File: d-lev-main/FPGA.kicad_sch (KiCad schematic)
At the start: 6 parts, among them J2 Tag-Connect TC2030-NL, U3 AC608, U4 25LCxxx

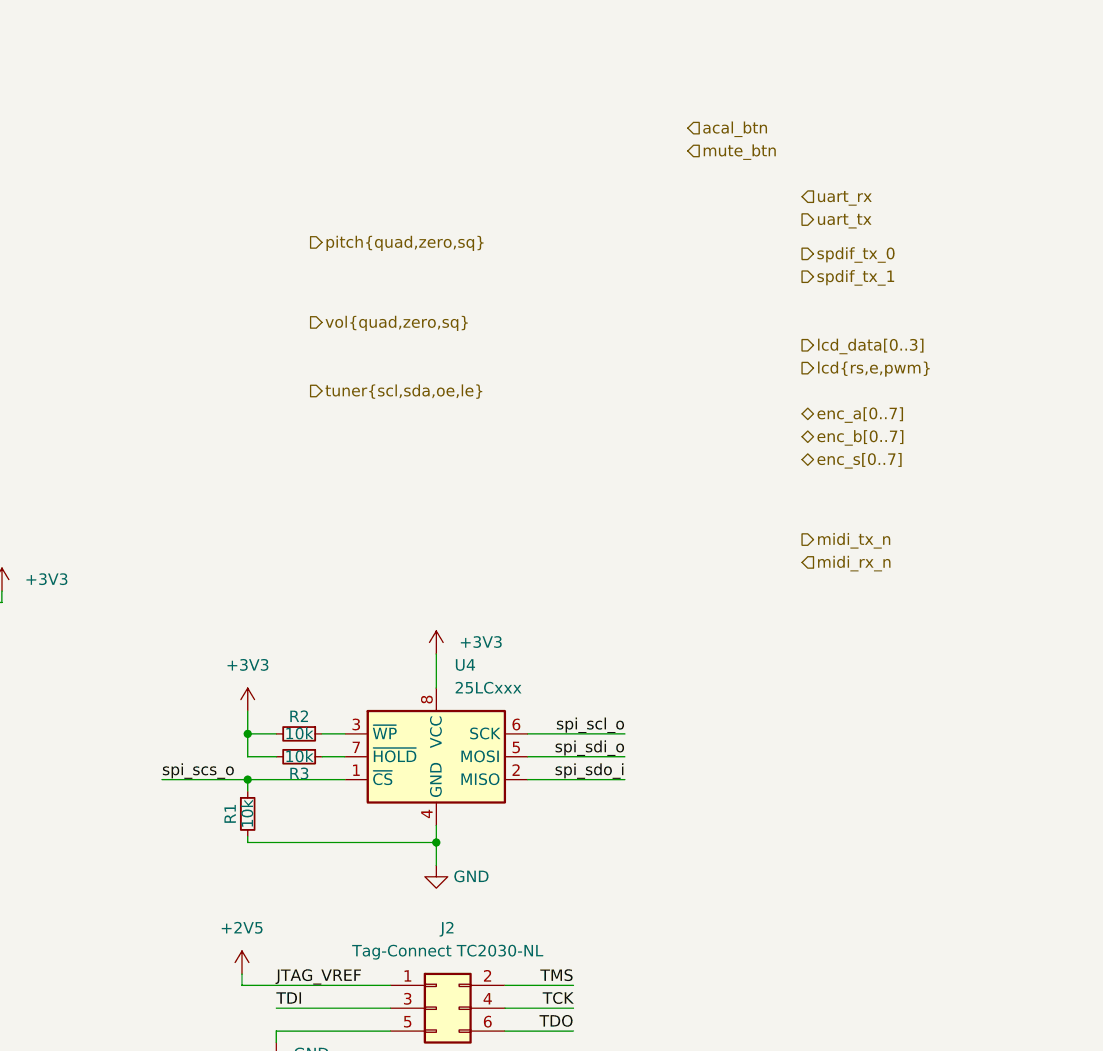
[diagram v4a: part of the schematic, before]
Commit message: Level shifters and rearrange encoders
* WIP: use net buses more effectively to organize encoder signals
* Add application note for level shifters
* Add level shifters for UART, change MIDI level shifter BJT to FET
* Add MIDI_HI pull-up on d-lev-io board
* Add/change some footprints
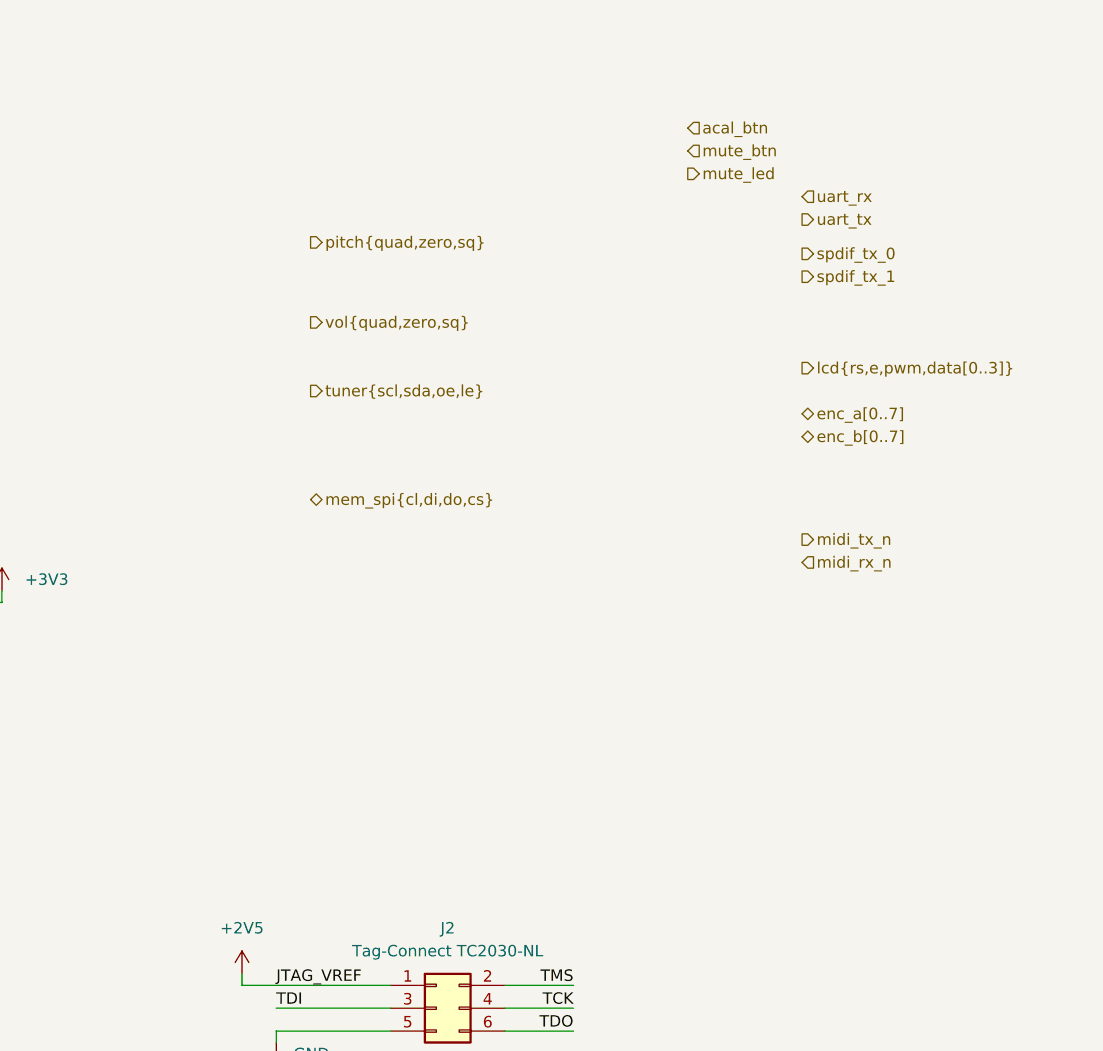
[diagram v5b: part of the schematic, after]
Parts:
- removed R1, R2, R3: 10k, symbol Device:R_Small
- removed U4: 25LCxxx, Package_SO:SOIC-8W_5.3x5.3mm_P1.27mm, symbol Memory_EEPROM:25LCxxx

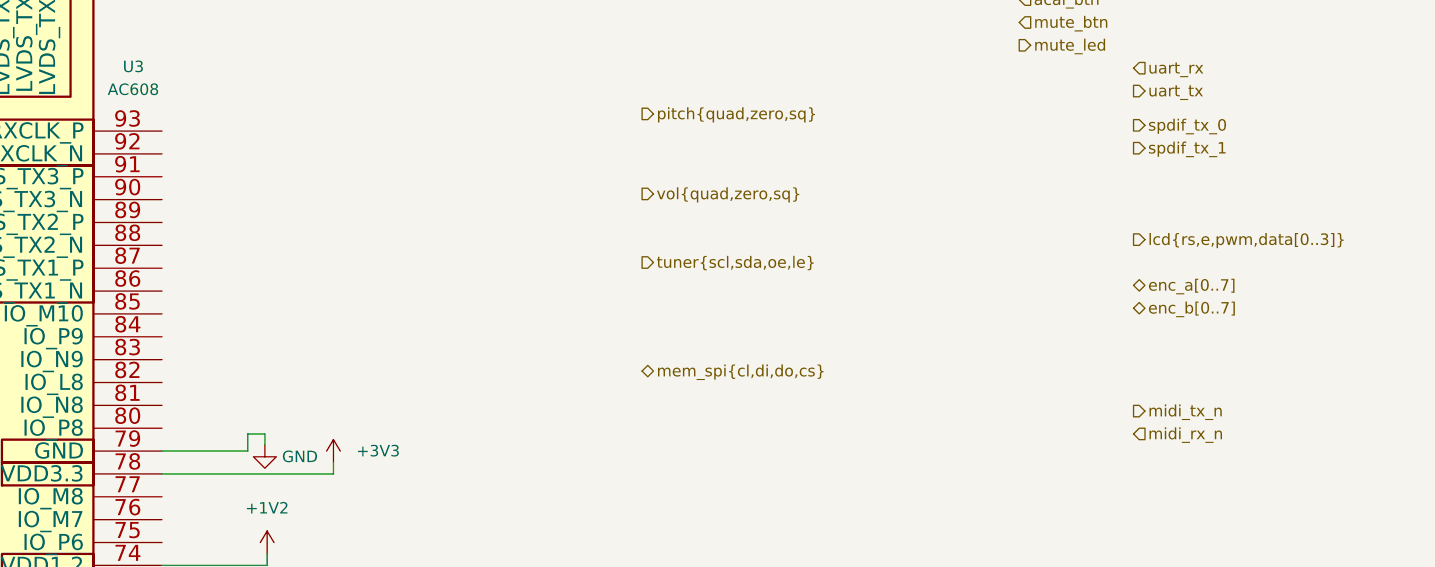
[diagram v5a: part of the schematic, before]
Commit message: more encoder bus mangling
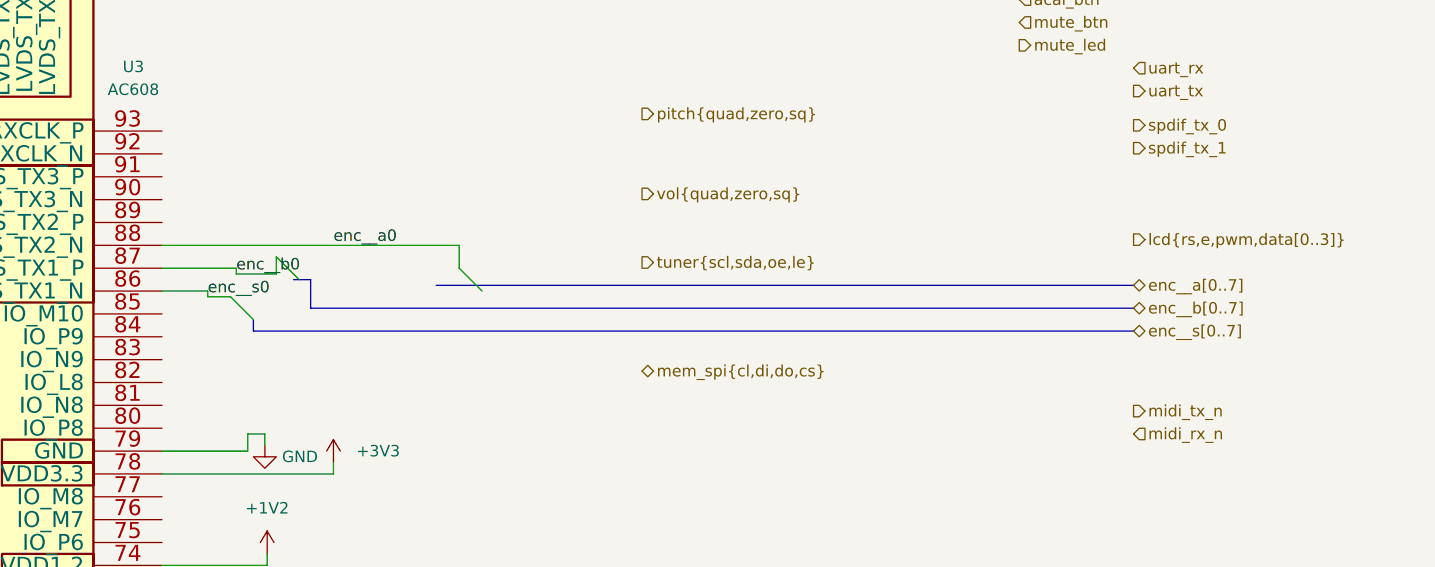
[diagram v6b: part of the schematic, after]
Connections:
- net enc__s0: now reaches U3.86 (LVDS_TX1_N)
- net enc__b0: now reaches U3.87 (LVDS_TX1_P)
- net enc__a0: now reaches U3.88 (LVDS_TX2_N)
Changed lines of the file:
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@@
 (kicad_sch (version 20230121) (generator eeschema)
   (paper "A4")
+  (bus_alias "lcdpins" (members "lcd{rs,e,pwm,data[0..3]}"))
   (bus_alias "tuner" (members "scl" "sda" "oe" "le"))
-  (bus_alias "lcdpins" (members "lcd{rs,e,pwm,data[0..3]}"))
+  (bus_entry (at 158.75 81.915) (size -2.54 -2.54)
+    (stroke (width 0) (type default))
+  )
+  (bus_entry (at 179.07 83.185) (size -2.54 -2.54)
+    (stroke (width 0) (type default))
+  )
+  (bus_entry (at 153.67 86.36) (size -2.54 -2.54)
+    (stroke (width 0) (type default))
+  )
+  (wire (pts (xy 156.21 79.375) (xy 156.21 81.28))
+    (stroke (width 0) (type default))
+  )
   (wire (pts (xy 218.44 151.13) (xy 226.06 151.13))
     (stroke (width 0) (type default))
@@
     (stroke (width 0) (type default))
   )
+  (wire (pts (xy 156.21 81.28) (xy 151.765 81.28))
+    (stroke (width 0) (type default))
+  )
   (wire (pts (xy 155.194 113.665) (xy 155.194 112.395))
     (stroke (width 0) (type default))
@@
     (stroke (width 0) (type default))
   )
+  (wire (pts (xy 151.765 80.645) (xy 151.765 81.28))
+    (stroke (width 0) (type default))
+  )
+  (wire (pts (xy 148.59 83.185) (xy 148.59 83.82))
+    (stroke (width 0) (type default))
+  )
+  (bus (pts (xy 251.46 87.63) (xy 153.67 87.63))
+    (stroke (width 0) (type default))
+  )
   (wire (pts (xy 100.33 36.195) (xy 100.33 37.465))
     (stroke (width 0) (type default))
   )
+  (bus (pts (xy 153.67 86.36) (xy 153.67 87.63))
+    (stroke (width 0) (type default))
+  )
   (wire (pts (xy 34.29 102.235) (xy 34.29 100.965))
     (stroke (width 0) (type default))
@@
     (stroke (width 0) (type default))
   )
+  (wire (pts (xy 176.53 80.645) (xy 176.53 78.105))
+    (stroke (width 0) (type default))
+  )
   (wire (pts (xy 92.71 175.895) (xy 92.71 174.625))
     (stroke (width 0) (type default))
@@
     (stroke (width 0) (type default))
   )
+  (wire (pts (xy 143.51 78.105) (xy 176.53 78.105))
+    (stroke (width 0) (type default))
+  )
   (wire (pts (xy 97.79 164.465) (xy 97.79 167.005))
     (stroke (width 0) (type default))
@@
     (stroke (width 0) (type default))
   )
+  (bus (pts (xy 158.75 81.915) (xy 160.02 81.915))
+    (stroke (width 0) (type default))
+  )
+  (bus (pts (xy 158.115 81.915) (xy 158.75 81.915))
+    (stroke (width 0) (type default))
+  )
+  (bus (pts (xy 251.46 85.09) (xy 160.02 85.09))
+    (stroke (width 0) (type default))
+  )
+  (wire (pts (xy 143.51 83.185) (xy 148.59 83.185))
+    (stroke (width 0) (type default))
+  )
   (wire (pts (xy 153.035 116.205) (xy 143.51 116.205))
     (stroke (width 0) (type default))
@@
     (stroke (width 0) (type default))
   )
+  (wire (pts (xy 143.51 80.645) (xy 151.765 80.645))
+    (stroke (width 0) (type default))
+  )
+  (wire (pts (xy 148.59 83.82) (xy 151.13 83.82))
+    (stroke (width 0) (type default))
+  )
   (wire (pts (xy 125.73 164.465) (xy 125.73 174.625))
     (stroke (width 0) (type default))
@@
     (stroke (width 0) (type default))
   )
+  (bus (pts (xy 160.02 85.09) (xy 160.02 81.915))
+    (stroke (width 0) (type default))
+  )
+  (bus (pts (xy 173.99 82.55) (xy 251.46 82.55))
+    (stroke (width 0) (type default))
+  )
   (label "TCK" (at 226.06 148.59 180) (fields_autoplaced)
     (effects (font (size 1.27 1.27)) (justify right bottom))
   )
+  (label "enc__a0" (at 162.56 78.105 0)
+    (effects (font (size 1.27 1.27)) (justify left bottom))
+  )
   (label "TDI" (at 193.04 148.59 0) (fields_autoplaced)
     (effects (font (size 1.27 1.27)) (justify left bottom))
@@
     (effects (font (size 1.27 1.27)) (justify right bottom))
   )
+  (label "enc__b0" (at 151.765 81.28 0)
+    (effects (font (size 1.27 1.27)) (justify left bottom))
+  )
+  (label "enc__s0" (at 148.59 83.82 0)
+    (effects (font (size 1.27 1.27)) (justify left bottom))
+  )
   (label "TCK" (at 125.73 174.625 90) (fields_autoplaced)
     (effects (font (size 1.27 1.27)) (justify left bottom))
@@
     (effects (font (size 1.27 1.27)) (justify left))
   )
+  (hierarchical_label "enc__s[0..7]" (shape bidirectional) (at 251.46 87.63 0) (fields_autoplaced)
+    (effects (font (size 1.27 1.27)) (justify left))
+  )
   (hierarchical_label "lcd{rs,e,pwm,data[0..3]}" (shape output) (at 251.46 77.47 0) (fields_autoplaced)
     (effects (font (size 1.27 1.27)) (justify left))
@@
     (effects (font (size 1.27 1.27)) (justify left))
   )
-  (hierarchical_label "enc_b[0..7]" (shape bidirectional) (at 251.46 85.09 0) (fields_autoplaced)
-    (effects (font (size 1.27 1.27)) (justify left))
-  )
-  (hierarchical_label "enc_a[0..7]" (shape bidirectional) (at 251.46 82.55 0) (fields_autoplaced)
-    (effects (font (size 1.27 1.27)) (justify left))
-  )
+  (hierarchical_label "enc__b[0..7]" (shape bidirectional) (at 251.46 85.09 0) (fields_autoplaced)
+    (effects (font (size 1.27 1.27)) (justify left))
+  )
+  (hierarchical_label "enc__a[0..7]" (shape bidirectional) (at 251.46 82.55 0) (fields_autoplaced)
+    (effects (font (size 1.27 1.27)) (justify left))
+  )

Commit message: Small changes to 3D models and footprints; fixed bus routing of encoder signals
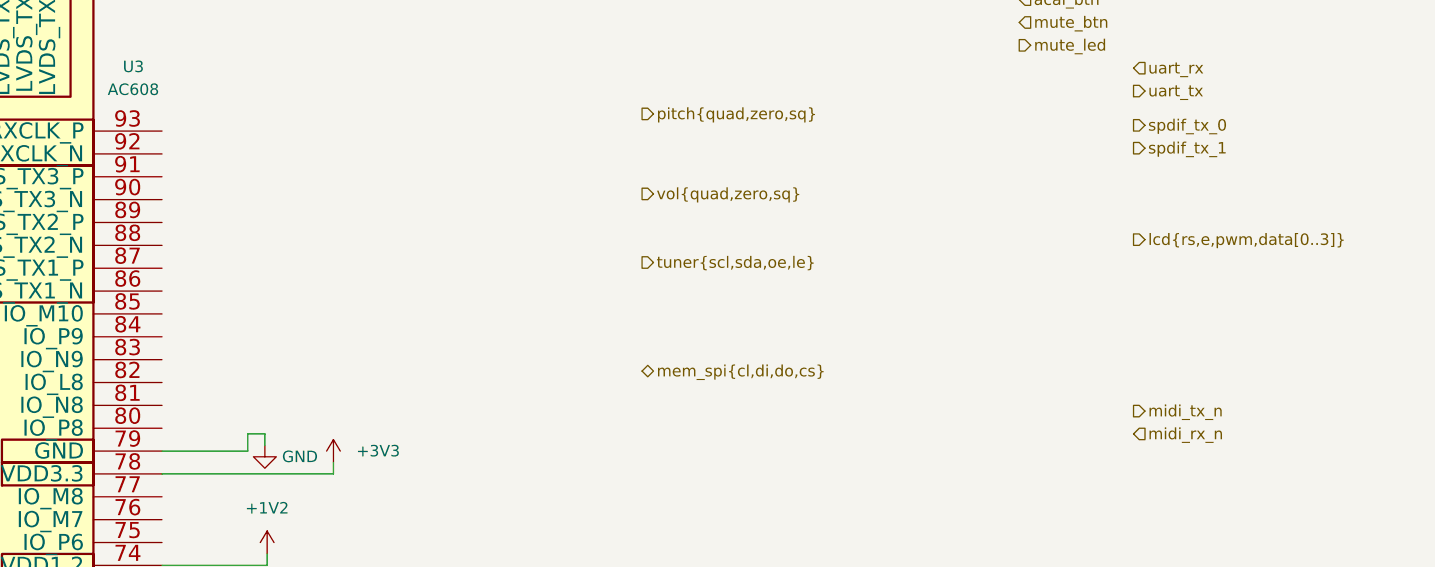
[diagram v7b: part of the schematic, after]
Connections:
- net enc__a0: no longer names the net of U3.88 (LVDS_TX2_N)
- net enc__b0: no longer names the net of U3.87 (LVDS_TX1_P)
- net enc__s0: no longer names the net of U3.86 (LVDS_TX1_N)
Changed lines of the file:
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@@
   (bus_alias "lcdpins" (members "lcd{rs,e,pwm,data[0..3]}"))
   (bus_alias "tuner" (members "scl" "sda" "oe" "le"))
-  (bus_entry (at 158.75 81.915) (size -2.54 -2.54)
-    (stroke (width 0) (type default))
-  )
-  (bus_entry (at 179.07 83.185) (size -2.54 -2.54)
-    (stroke (width 0) (type default))
-  )
-  (bus_entry (at 153.67 86.36) (size -2.54 -2.54)
-    (stroke (width 0) (type default))
-  )
-  (wire (pts (xy 156.21 79.375) (xy 156.21 81.28))
-    (stroke (width 0) (type default))
-  )
   (wire (pts (xy 218.44 151.13) (xy 226.06 151.13))
     (stroke (width 0) (type default))
@@
     (stroke (width 0) (type default))
   )
-  (wire (pts (xy 156.21 81.28) (xy 151.765 81.28))
-    (stroke (width 0) (type default))
-  )
   (wire (pts (xy 155.194 113.665) (xy 155.194 112.395))
     (stroke (width 0) (type default))
@@
     (stroke (width 0) (type default))
   )
-  (wire (pts (xy 151.765 80.645) (xy 151.765 81.28))
-    (stroke (width 0) (type default))
-  )
-  (wire (pts (xy 148.59 83.185) (xy 148.59 83.82))
-    (stroke (width 0) (type default))
-  )
-  (bus (pts (xy 251.46 87.63) (xy 153.67 87.63))
-    (stroke (width 0) (type default))
-  )
   (wire (pts (xy 100.33 36.195) (xy 100.33 37.465))
-    (stroke (width 0) (type default))
-  )
-  (bus (pts (xy 153.67 86.36) (xy 153.67 87.63))
     (stroke (width 0) (type default))
   )
@@
     (stroke (width 0) (type default))
   )
-  (wire (pts (xy 176.53 80.645) (xy 176.53 78.105))
-    (stroke (width 0) (type default))
-  )
   (wire (pts (xy 92.71 175.895) (xy 92.71 174.625))
     (stroke (width 0) (type default))
@@
   )
   (wire (pts (xy 154.94 99.06) (xy 154.94 100.33))
-    (stroke (width 0) (type default))
-  )
-  (wire (pts (xy 143.51 78.105) (xy 176.53 78.105))
     (stroke (width 0) (type default))
   )
@@
     (stroke (width 0) (type default))
   )
-  (bus (pts (xy 158.75 81.915) (xy 160.02 81.915))
-    (stroke (width 0) (type default))
-  )
-  (bus (pts (xy 158.115 81.915) (xy 158.75 81.915))
-    (stroke (width 0) (type default))
-  )
-  (bus (pts (xy 251.46 85.09) (xy 160.02 85.09))
-    (stroke (width 0) (type default))
-  )
-  (wire (pts (xy 143.51 83.185) (xy 148.59 83.185))
-    (stroke (width 0) (type default))
-  )
   (wire (pts (xy 153.035 116.205) (xy 143.51 116.205))
     (stroke (width 0) (type default))
   )
   (wire (pts (xy 34.29 100.965) (xy 41.91 100.965))
-    (stroke (width 0) (type default))
-  )
-  (wire (pts (xy 143.51 80.645) (xy 151.765 80.645))
-    (stroke (width 0) (type default))
-  )
-  (wire (pts (xy 148.59 83.82) (xy 151.13 83.82))
     (stroke (width 0) (type default))
   )
@@
     (stroke (width 0) (type default))
   )
-  (bus (pts (xy 160.02 85.09) (xy 160.02 81.915))
-    (stroke (width 0) (type default))
-  )
-  (bus (pts (xy 173.99 82.55) (xy 251.46 82.55))
-    (stroke (width 0) (type default))
-  )
   (label "TCK" (at 226.06 148.59 180) (fields_autoplaced)
     (effects (font (size 1.27 1.27)) (justify right bottom))
-  )
-  (label "enc__a0" (at 162.56 78.105 0)
-    (effects (font (size 1.27 1.27)) (justify left bottom))
   )
   (label "TDI" (at 193.04 148.59 0) (fields_autoplaced)
@@
     (effects (font (size 1.27 1.27)) (justify right bottom))
   )
-  (label "enc__b0" (at 151.765 81.28 0)
-    (effects (font (size 1.27 1.27)) (justify left bottom))
-  )
-  (label "enc__s0" (at 148.59 83.82 0)
-    (effects (font (size 1.27 1.27)) (justify left bottom))
-  )
   (label "TCK" (at 125.73 174.625 90) (fields_autoplaced)
     (effects (font (size 1.27 1.27)) (justify left bottom))
@@
     (effects (font (size 1.27 1.27)) (justify left))
   )
-  (hierarchical_label "enc__s[0..7]" (shape bidirectional) (at 251.46 87.63 0) (fields_autoplaced)
-    (effects (font (size 1.27 1.27)) (justify left))
-  )
   (hierarchical_label "lcd{rs,e,pwm,data[0..3]}" (shape output) (at 251.46 77.47 0) (fields_autoplaced)
     (effects (font (size 1.27 1.27)) (justify left))
@@
     (effects (font (size 1.27 1.27)) (justify left))
   )
-  (hierarchical_label "enc__b[0..7]" (shape bidirectional) (at 251.46 85.09 0) (fields_autoplaced)
-    (effects (font (size 1.27 1.27)) (justify left))
-  )
-  (hierarchical_label "enc__a[0..7]" (shape bidirectional) (at 251.46 82.55 0) (fields_autoplaced)
-    (effects (font (size 1.27 1.27)) (justify left))
-  )
